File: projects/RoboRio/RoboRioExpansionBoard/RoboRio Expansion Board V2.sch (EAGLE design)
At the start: 83 parts, among them CN1 PROP_PLUG, J1 RRINTERFACE-FEMALE, J2 MICROSD, Q1 5.0 MHz, T1 NPN-SOT416, U1 P8X32A-Q44, U2 24LC256ST, U3 FT232RFTR232R, U4 MC1525TO

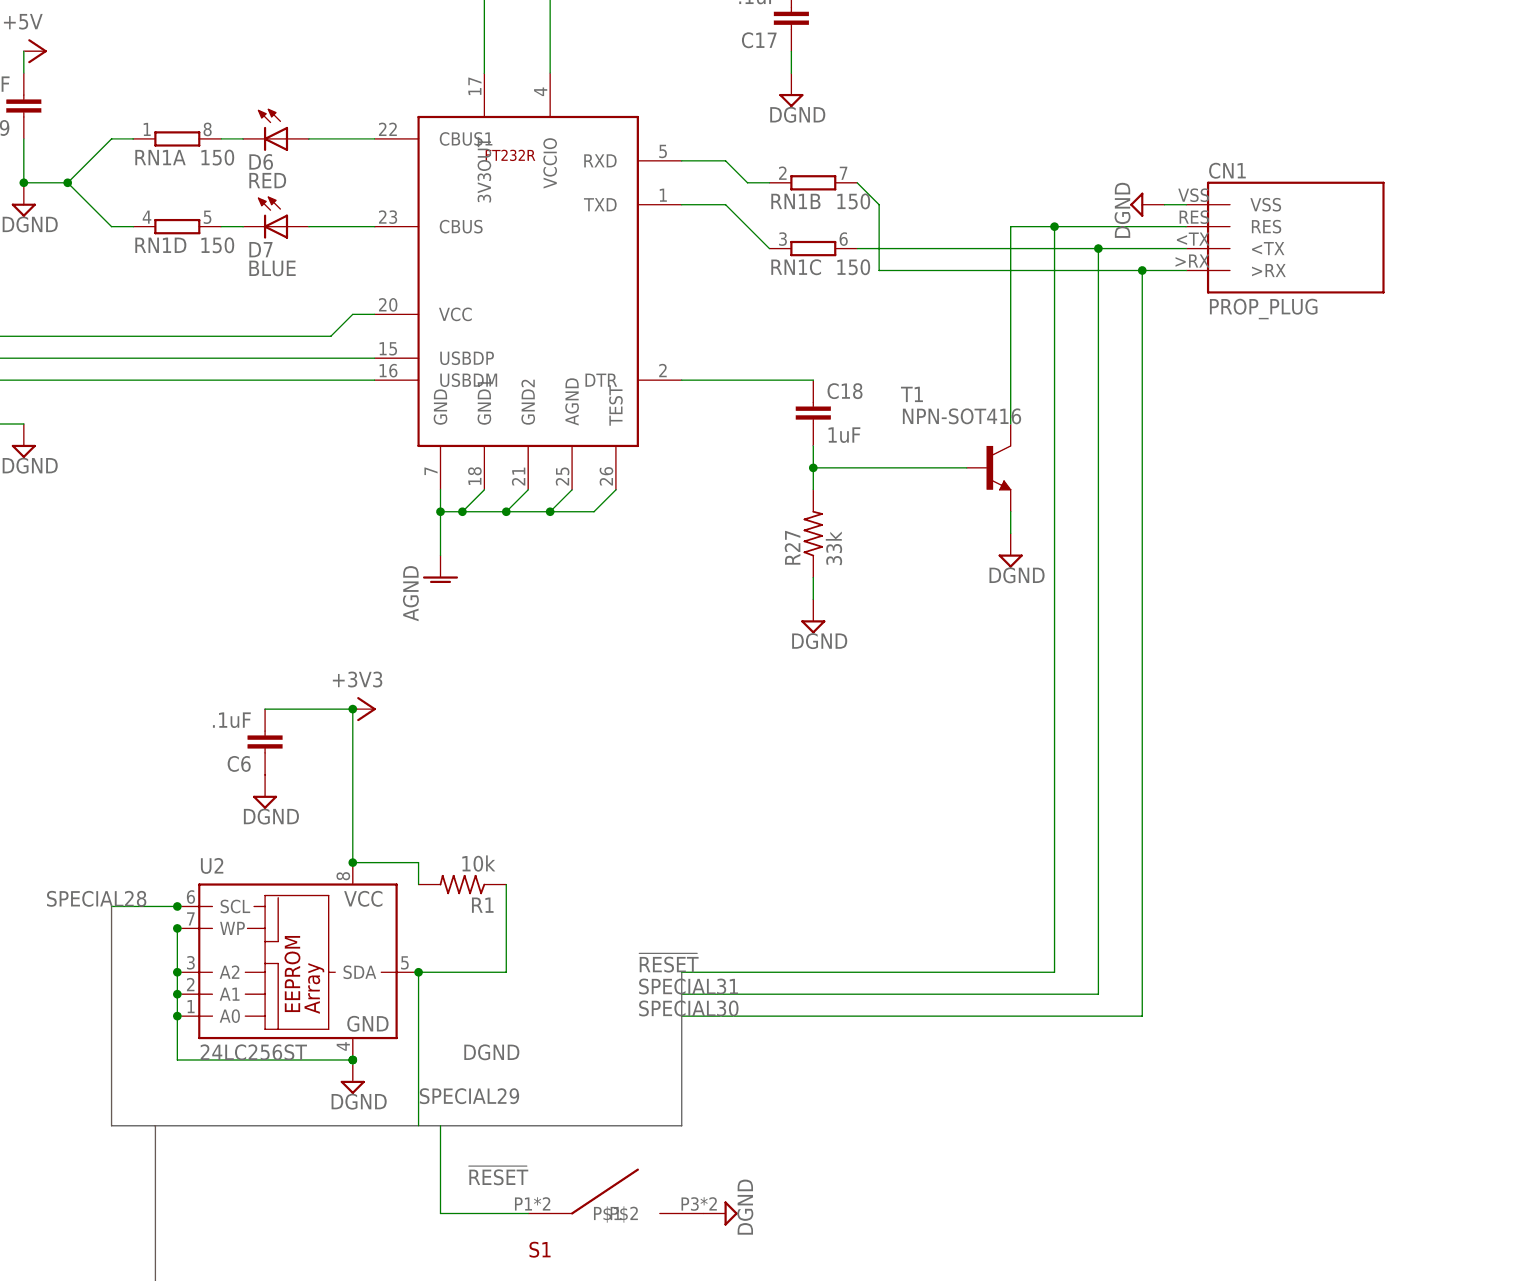
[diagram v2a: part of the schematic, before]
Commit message: Removed Prop Plug connector
Since we now have USB, it isn't needed.
Also fixed a straggling Analog GND issue.
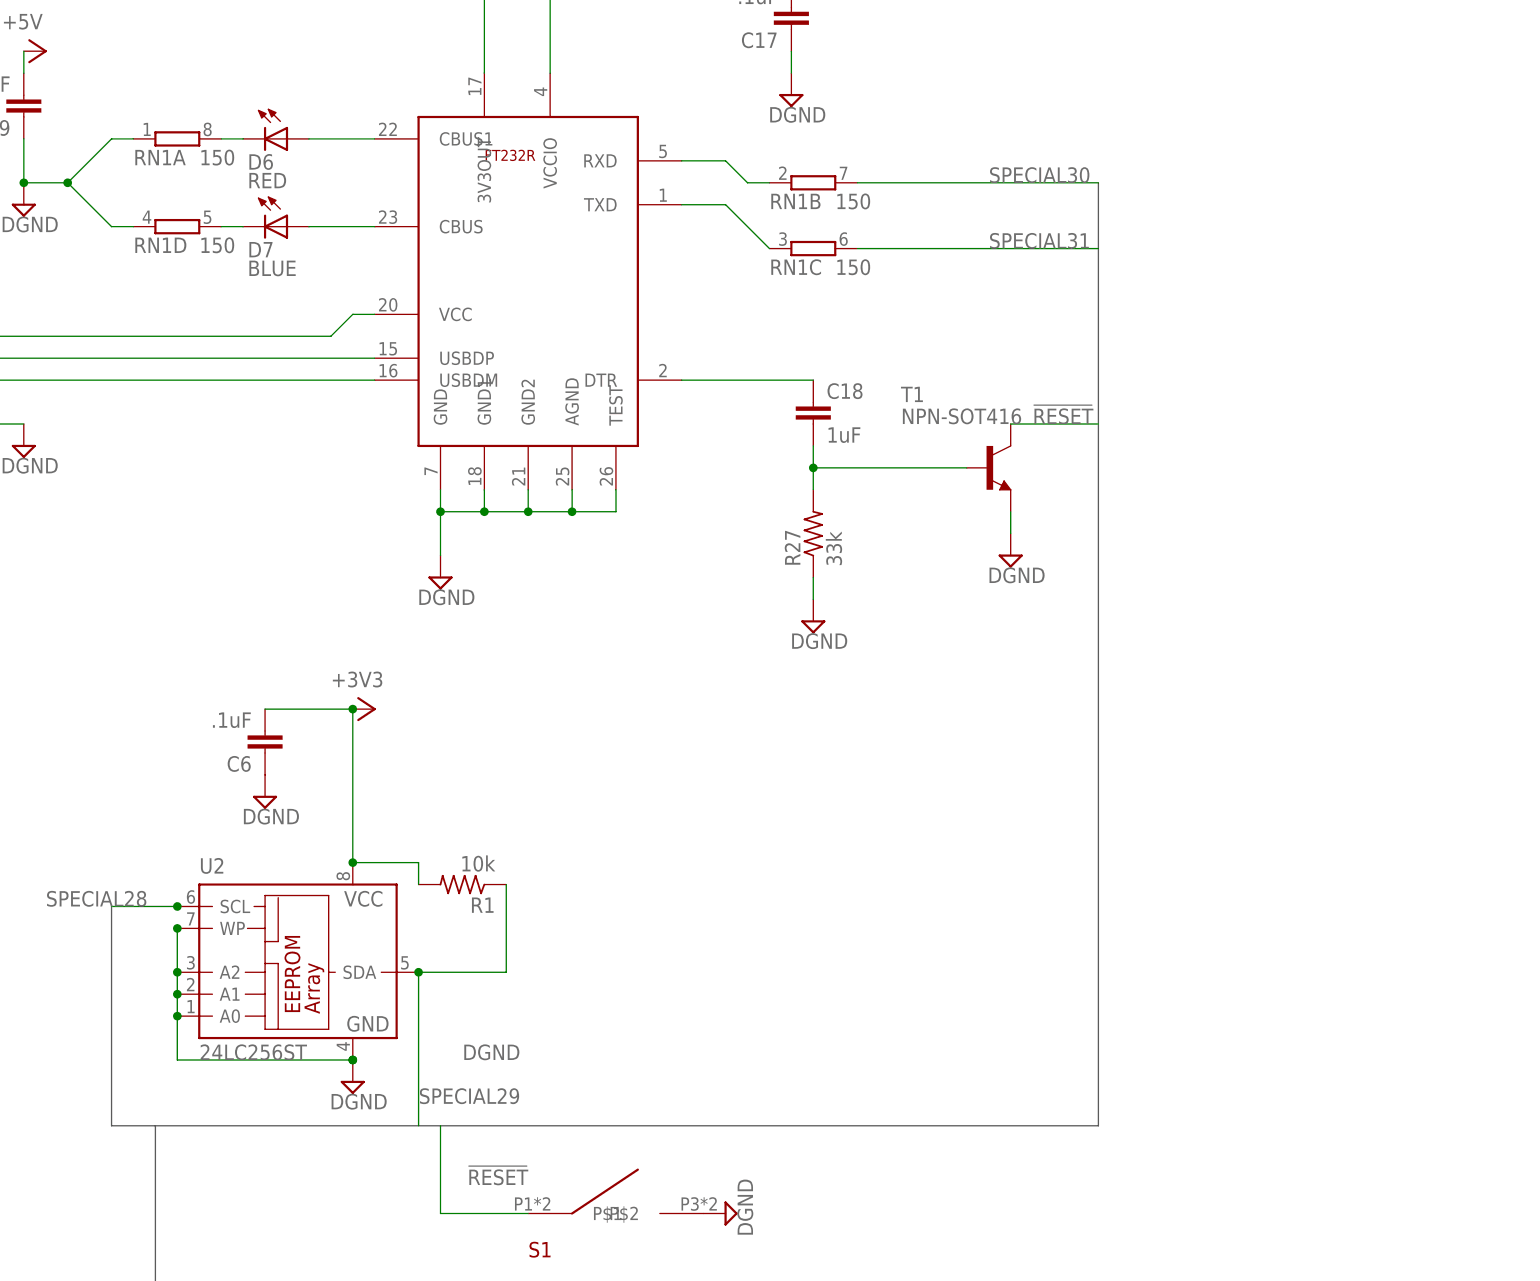
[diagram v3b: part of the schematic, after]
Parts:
- removed CN1: PROP_PLUG, PropPlug:PROP_PLUG
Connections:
- net !RESET: no longer CN1.RES
- net AGND: no longer U3.AGND, U3.GND, U3.GND1, U3.GND2, U3.TEST
- net DGND: now also U3.AGND, U3.GND, U3.GND1, U3.GND2, U3.TEST; no longer CN1.VSS
- net SPECIAL30: no longer CN1.>RX
- net SPECIAL31: no longer CN1.<TX
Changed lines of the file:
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@@
 <part name="C17" library="resistor" deviceset="C-EU" device="C0603K" value=".1uF"/>
 <part name="SUPPLY6" library="supply2" deviceset="DGND" device=""/>
-<part name="CN1" library="PropPlug" deviceset="PROP_PLUG" device=""/>
-<part name="AGND4" library="supply1" deviceset="AGND" device=""/>
 <part name="R27" library="resistor" deviceset="R-US_" device="R0603" value="33k"/>
 <part name="C18" library="resistor" deviceset="C-EU" device="C0603K" value="1uF"/>
@@
 <part name="SUPPLY11" library="supply2" deviceset="DGND" device=""/>
 <part name="SUPPLY19" library="supply2" deviceset="DGND" device=""/>
-<part name="SUPPLY20" library="supply2" deviceset="DGND" device=""/>
 <part name="SUPPLY21" library="supply2" deviceset="DGND" device=""/>
 <part name="SUPPLY22" library="supply2" deviceset="DGND" device=""/>
@@
 <part name="RN2" library="resistor-dil" deviceset="4R-N" device="0402ARV341" value="150"/>
 <part name="RN3" library="resistor-dil" deviceset="4R-N" device="0402ARV341" value="150"/>
+<part name="SUPPLY20" library="supply2" deviceset="DGND" device=""/>
 </parts>
 <sheets>
@@
 <instance part="C17" gate="G$1" x="167.64" y="261.62" rot="R180"/>
 <instance part="SUPPLY6" gate="G$1" x="167.64" y="254"/>
-<instance part="CN1" gate="G$1" x="215.9" y="243.84"/>
-<instance part="AGND4" gate="VR1" x="127" y="198.12"/>
 <instance part="R27" gate="G$1" x="170.18" y="203.2" rot="R90"/>
 <instance part="C18" gate="G$1" x="170.18" y="218.44"/>
@@
 <instance part="SUPPLY11" gate="G$1" x="78.74" y="241.3"/>
 <instance part="SUPPLY19" gate="G$1" x="193.04" y="200.66"/>
-<instance part="SUPPLY20" gate="G$1" x="208.28" y="241.3" rot="R270"/>
 <instance part="SUPPLY21" gate="G$1" x="261.62" y="-63.5" rot="R270"/>
 <instance part="SUPPLY22" gate="G$1" x="261.62" y="-88.9" rot="R270"/>
@@
 <instance part="RN3" gate="C" x="12.7" y="111.76"/>
 <instance part="RN3" gate="D" x="12.7" y="101.6"/>
+<instance part="SUPPLY20" gate="G$1" x="127" y="198.12"/>
 </instances>
 <busses>
@@
 <wire x1="93.98" y1="134.62" x2="88.9" y2="134.62" width="0.762" layer="92"/>
 <wire x1="88.9" y1="134.62" x2="88.9" y2="160.02" width="0.762" layer="92"/>
-<wire x1="93.98" y1="134.62" x2="154.94" y2="134.62" width="0.762" layer="92"/>
-<wire x1="154.94" y1="134.62" x2="154.94" y2="152.4" width="0.762" layer="92"/>
+<wire x1="93.98" y1="134.62" x2="203.2" y2="134.62" width="0.762" layer="92"/>
+<wire x1="203.2" y1="134.62" x2="203.2" y2="243.84" width="0.762" layer="92"/>
 <wire x1="93.98" y1="134.62" x2="93.98" y2="101.6" width="0.762" layer="92"/>
 <wire x1="93.98" y1="101.6" x2="58.42" y2="66.04" width="0.762" layer="92"/>
@@
 <net name="SPECIAL30" class="0">
 <segment>
-<label x="149.86" y="147.32" size="1.778" layer="95"/>
-<pinref part="CN1" gate="G$1" pin="&gt;RX"/>
-<wire x1="175.26" y1="243.84" x2="177.8" y2="241.3" width="0.1524" layer="91"/>
-<wire x1="177.8" y1="241.3" x2="177.8" y2="233.68" width="0.1524" layer="91"/>
-<wire x1="177.8" y1="233.68" x2="208.28" y2="233.68" width="0.1524" layer="91"/>
-<wire x1="208.28" y1="233.68" x2="213.36" y2="233.68" width="0.1524" layer="91"/>
-<wire x1="208.28" y1="233.68" x2="208.28" y2="147.32" width="0.1524" layer="91"/>
-<wire x1="208.28" y1="147.32" x2="154.94" y2="147.32" width="0.1524" layer="91"/>
-<junction x="208.28" y="233.68"/>
+<wire x1="175.26" y1="243.84" x2="203.2" y2="243.84" width="0.1524" layer="91"/>
 <pinref part="RN1" gate="B" pin="2"/>
+<label x="190.5" y="243.84" size="1.778" layer="95"/>
 </segment>
 <segment>
@@
 <net name="SPECIAL31" class="0">
 <segment>
-<label x="149.86" y="149.86" size="1.778" layer="95"/>
-<pinref part="CN1" gate="G$1" pin="&lt;TX"/>
 <wire x1="175.26" y1="236.22" x2="203.2" y2="236.22" width="0.1524" layer="91"/>
-<wire x1="203.2" y1="236.22" x2="213.36" y2="236.22" width="0.1524" layer="91"/>
-<wire x1="203.2" y1="236.22" x2="203.2" y2="149.86" width="0.1524" layer="91"/>
-<wire x1="203.2" y1="149.86" x2="154.94" y2="149.86" width="0.1524" layer="91"/>
-<junction x="203.2" y="236.22"/>
 <pinref part="RN1" gate="C" pin="2"/>
+<label x="190.5" y="236.22" size="1.778" layer="95"/>
 </segment>
 <segment>
@@
 <net name="!RESET" class="0">
 <segment>
-<label x="149.86" y="152.4" size="1.778" layer="95"/>
 <pinref part="T1" gate="G$1" pin="C"/>
-<wire x1="193.04" y1="215.9" x2="193.04" y2="238.76" width="0.1524" layer="91"/>
-<pinref part="CN1" gate="G$1" pin="RES"/>
-<wire x1="193.04" y1="238.76" x2="198.12" y2="238.76" width="0.1524" layer="91"/>
-<wire x1="198.12" y1="238.76" x2="213.36" y2="238.76" width="0.1524" layer="91"/>
-<wire x1="198.12" y1="238.76" x2="198.12" y2="152.4" width="0.1524" layer="91"/>
-<wire x1="198.12" y1="152.4" x2="154.94" y2="152.4" width="0.1524" layer="91"/>
-<junction x="198.12" y="238.76"/>
+<wire x1="193.04" y1="215.9" x2="203.2" y2="215.9" width="0.1524" layer="91"/>
+<label x="195.58" y="215.9" size="1.778" layer="95"/>
 </segment>
 <segment>
@@
 </segment>
 <segment>
-<pinref part="CN1" gate="G$1" pin="VSS"/>
-<wire x1="210.82" y1="241.3" x2="213.36" y2="241.3" width="0.1524" layer="91"/>
-<pinref part="SUPPLY20" gate="G$1" pin="DGND"/>
-</segment>
-<segment>
 <pinref part="ADC7" gate="G$1" pin="1"/>
 <pinref part="SUPPLY21" gate="G$1" pin="DGND"/>
@@
 <pinref part="ADC2" gate="G$1" pin="1"/>
 <pinref part="SUPPLY28" gate="G$1" pin="DGND"/>
+</segment>
+<segment>
+<wire x1="127" y1="200.66" x2="127" y2="205.74" width="0.1524" layer="91"/>
+<wire x1="127" y1="205.74" x2="127" y2="208.28" width="0.1524" layer="91"/>
+<wire x1="127" y1="205.74" x2="132.08" y2="205.74" width="0.1524" layer="91"/>
+<wire x1="132.08" y1="205.74" x2="132.08" y2="208.28" width="0.1524" layer="91"/>
+<wire x1="132.08" y1="205.74" x2="137.16" y2="205.74" width="0.1524" layer="91"/>
+<wire x1="137.16" y1="205.74" x2="137.16" y2="208.28" width="0.1524" layer="91"/>
+<wire x1="137.16" y1="205.74" x2="142.24" y2="205.74" width="0.1524" layer="91"/>
+<wire x1="142.24" y1="205.74" x2="142.24" y2="208.28" width="0.1524" layer="91"/>
+<wire x1="142.24" y1="205.74" x2="147.32" y2="205.74" width="0.1524" layer="91"/>
+<wire x1="147.32" y1="205.74" x2="147.32" y2="208.28" width="0.1524" layer="91"/>
+<junction x="132.08" y="205.74"/>
+<junction x="137.16" y="205.74"/>
+<junction x="142.24" y="205.74"/>
+<junction x="127" y="205.74"/>
+<pinref part="U3" gate="G$1" pin="AGND"/>
+<pinref part="U3" gate="G$1" pin="GND"/>
+<pinref part="U3" gate="G$1" pin="GND1"/>
+<pinref part="U3" gate="G$1" pin="GND2"/>
+<pinref part="U3" gate="G$1" pin="TEST"/>
+<pinref part="SUPPLY20" gate="G$1" pin="DGND"/>
 </segment>
 </net>
@@
 <junction x="-113.03" y="1.27"/>
 </segment>
-<segment>
-<pinref part="AGND4" gate="VR1" pin="AGND"/>
-<wire x1="127" y1="200.66" x2="127" y2="205.74" width="0.1524" layer="91"/>
-<wire x1="127" y1="205.74" x2="127" y2="208.28" width="0.1524" layer="91"/>
-<wire x1="127" y1="205.74" x2="129.54" y2="205.74" width="0.1524" layer="91"/>
-<wire x1="129.54" y1="205.74" x2="132.08" y2="208.28" width="0.1524" layer="91"/>
-<wire x1="129.54" y1="205.74" x2="134.62" y2="205.74" width="0.1524" layer="91"/>
-<wire x1="134.62" y1="205.74" x2="137.16" y2="208.28" width="0.1524" layer="91"/>
-<wire x1="134.62" y1="205.74" x2="139.7" y2="205.74" width="0.1524" layer="91"/>
-<wire x1="139.7" y1="205.74" x2="142.24" y2="208.28" width="0.1524" layer="91"/>
-<wire x1="139.7" y1="205.74" x2="144.78" y2="205.74" width="0.1524" layer="91"/>
-<wire x1="144.78" y1="205.74" x2="147.32" y2="208.28" width="0.1524" layer="91"/>
-<junction x="129.54" y="205.74"/>
-<junction x="134.62" y="205.74"/>
-<junction x="139.7" y="205.74"/>
-<junction x="127" y="205.74"/>
-<pinref part="U3" gate="G$1" pin="AGND"/>
-<pinref part="U3" gate="G$1" pin="GND"/>
-<pinref part="U3" gate="G$1" pin="GND1"/>
-<pinref part="U3" gate="G$1" pin="GND2"/>
-<pinref part="U3" gate="G$1" pin="TEST"/>
-</segment>
-</net>
+</net>
